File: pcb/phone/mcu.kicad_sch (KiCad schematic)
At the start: 22 parts, among them U1 STM32H743ZIT6, Y1 ECS-80-12-33Q-GN-TR

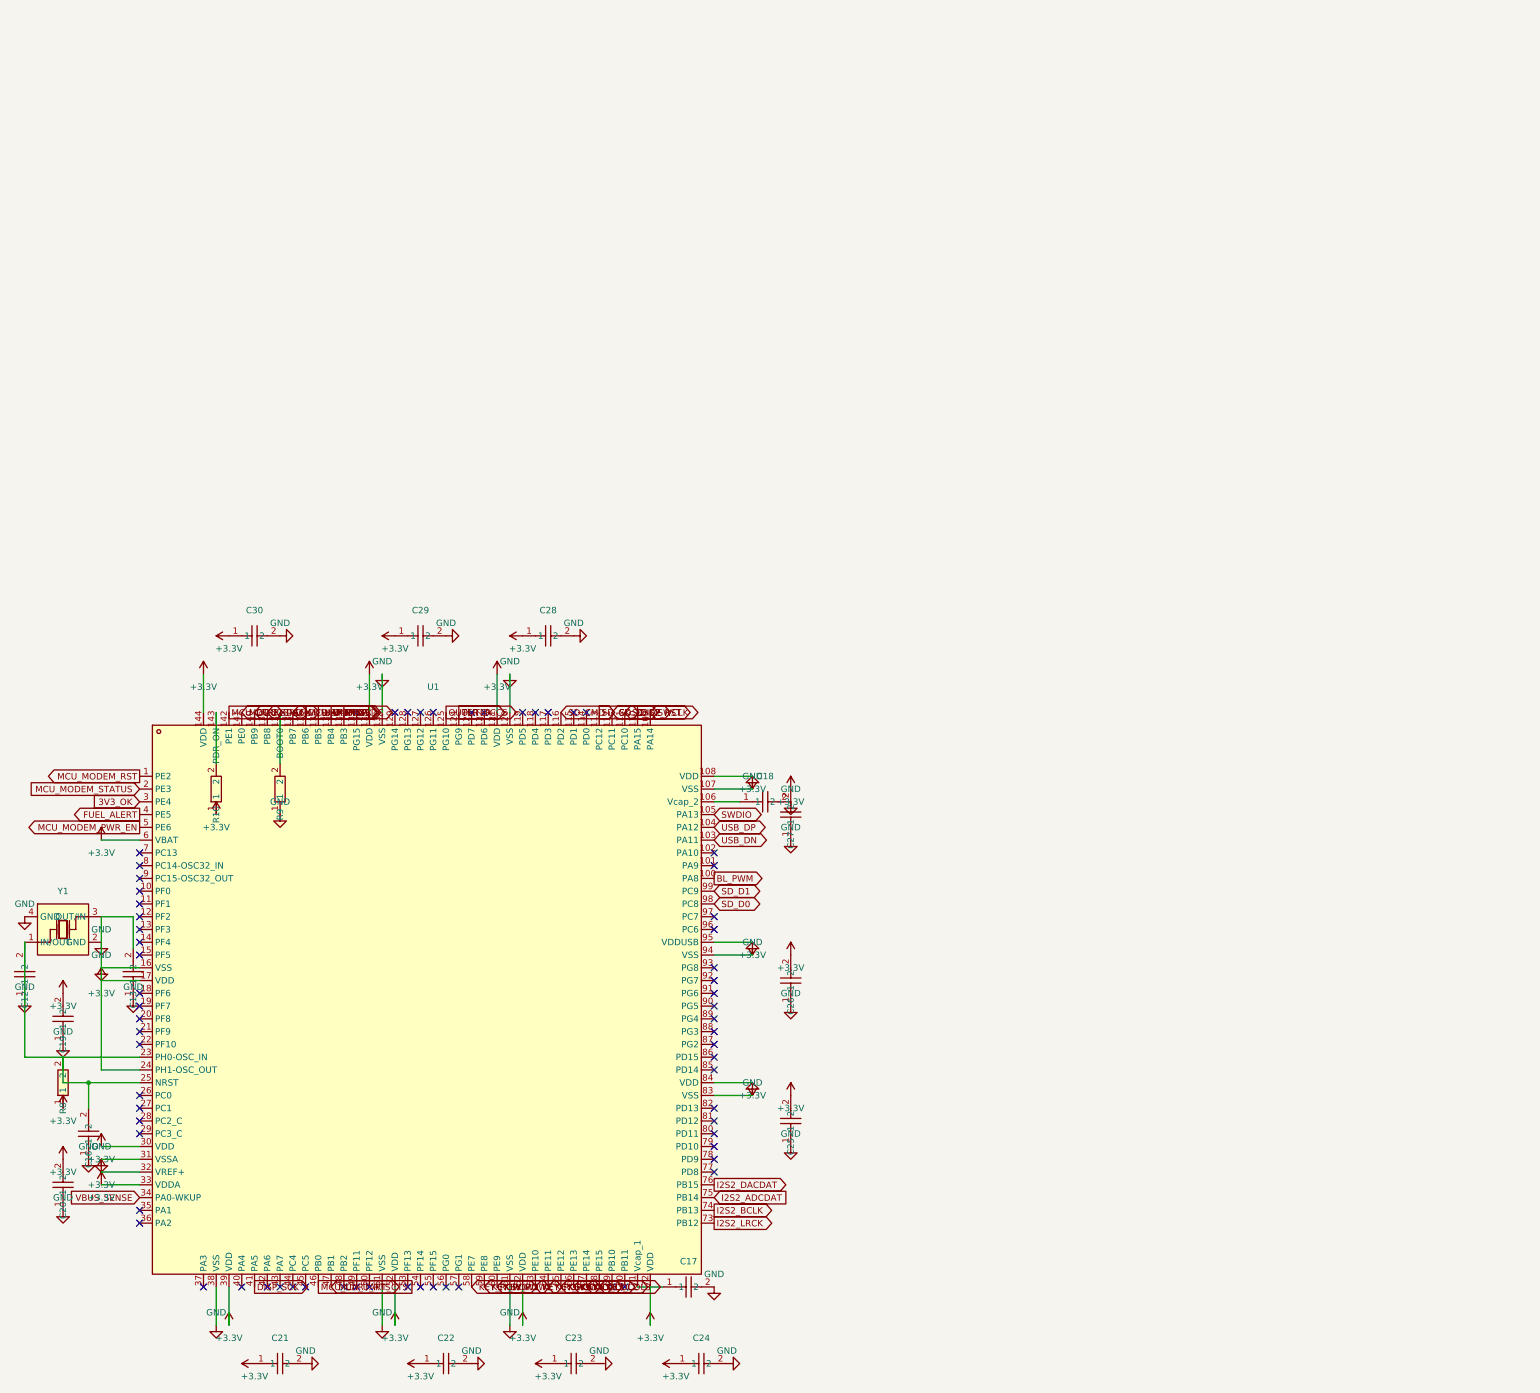
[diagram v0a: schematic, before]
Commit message: Phase 3.3: Complete modem sheet + MCU power symbol cleanup
Modem sheet (modem.kicad_sch):
- MPCIe socket (U2), TXB0108 level shifter (U8), bulk caps (C31/C32), pullup (R11)
- All 54 MPCIe pins wired: power, UART, PCM, USB, SIM, control signals
- Power symbol lib_symbols extracted from KiCad power library
- No PWR_FLAGs (power rails driven by root sheet regulators)
- 0 ERC errors on modem sheet

MCU sheet (mcu.kicad_sch):
- Fixed 14 overlapping power symbol clusters (2.54mm -> 5.08mm+ spacing)
- User manual pass: rotated and spaced components for readability
- ERC unchanged: 5 pre-existing root sheet errors, 0 MCU errors

Generated with [Devin](https://devin.ai)

Co-Authored-By: Devin <158243242+devin-ai-integration[bot]@users.noreply.github.com
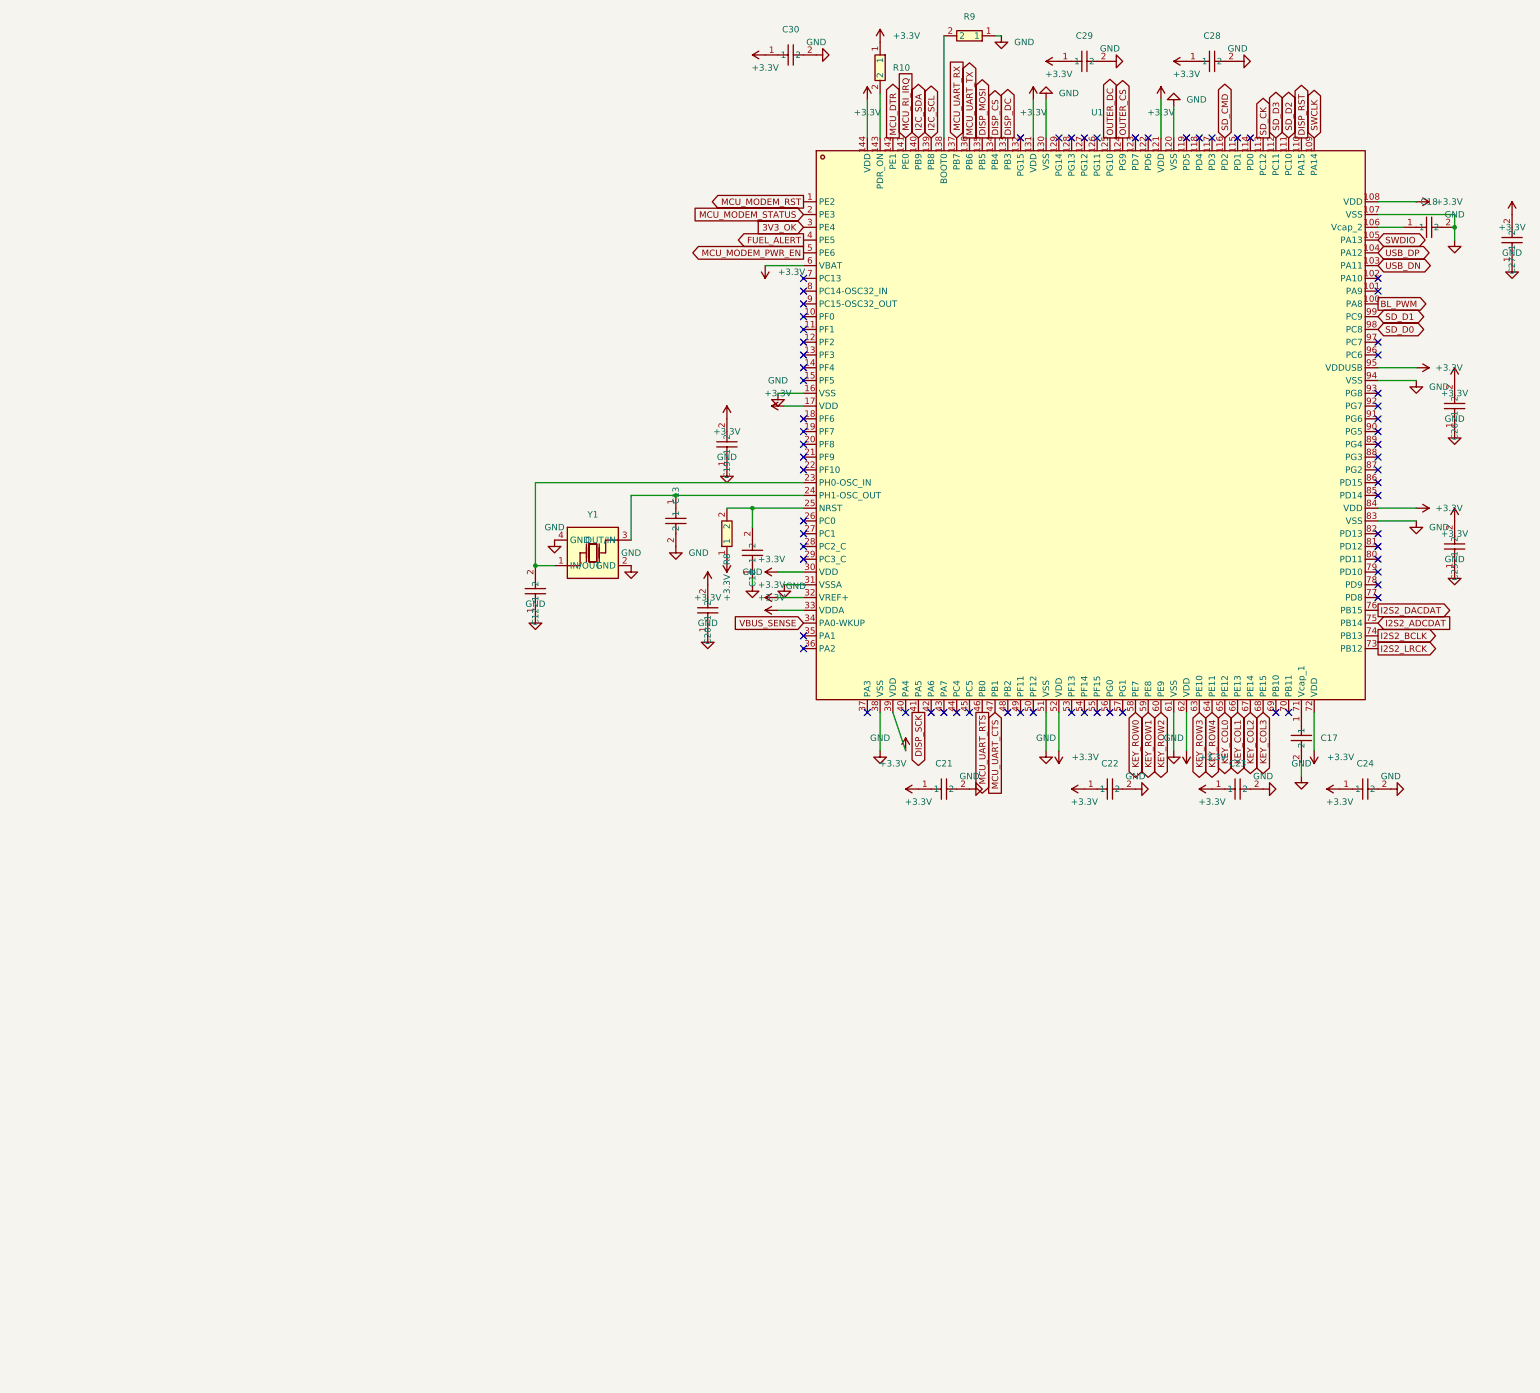
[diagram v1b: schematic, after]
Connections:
- net GND: now also C13.2; no longer C13.1
- net at U1.24 (PH1-OSC_OUT), Y1.3 (OUT/IN): now also C13.1; no longer C13.2
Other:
- moved on the sheet: C12, C13, C16, C17, C18, C19, C20, C21, C22, C23, C24, C25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

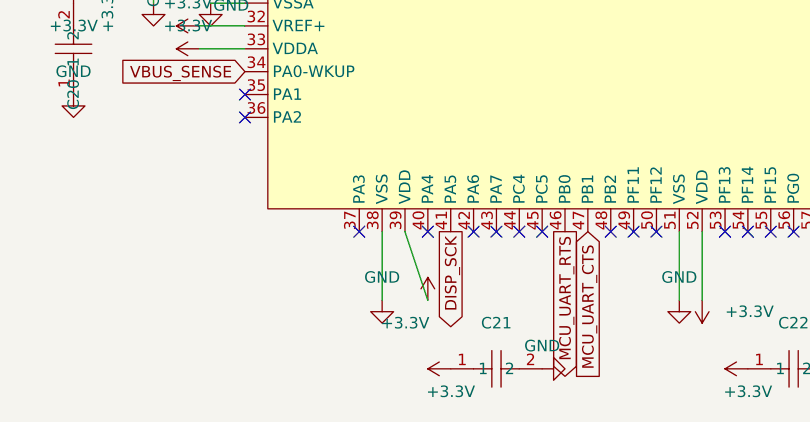
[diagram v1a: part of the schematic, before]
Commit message: User edits: keypad rewiring, sheet reorder, ERC severity reverts, R24 fix
Keypad (keypad.kicad_sch):
- Rotated all 20 switches 270 degrees for vertical contact orientation
- Wired all 4 pins on each switch (pins 1&2 to column, pins 3&4 to row)
- Removed all 37 no_connect markers on pins 3&4
- Cleaned up to 25.4mm (1-inch) grid spacing
- Added pull-down resistors to all 4 columns (was only KEY_COL3)

Root sheet (phone.kicad_sch):
- Reordered sub-sheet blocks (Display_Daughter before SIM_SD)
- Cleaned up PWR_FLAG symbol formatting/indentation
- Reordered PWR_FLAG and +BATT symbol placement

MCU sheet (mcu.kicad_sch):
- Repositioned +3.3V power symbol (#PWR32) at pin 190.5,200.66

Project settings (phone.kicad_pro):
- Reverted ERC suppressions: endpoint_off_grid, isolated_pin_label,
  lib_symbol_mismatch back to warning (want actual fixes, not ignores)
- Added SW2-20 to used designators
- Reordered sheets list (Display_Daughter before SIM_SD)

Other sheets (codec, display, display_daughter, sim_sd):
- KiCad editor reformatting upon save

Generated with [Devin](https://devin.ai)

Co-Authored-By: Devin <158243242+devin-ai-integration[bot]@users.noreply.github.com>
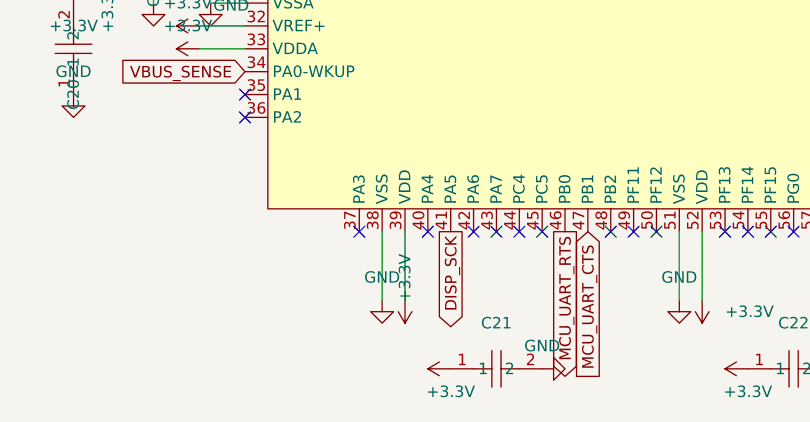
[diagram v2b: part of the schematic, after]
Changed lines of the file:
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@@
 	(wire
 		(pts
-			(xy 190.5 193.04) (xy 193.04 200.66)
+			(xy 190.5 193.04) (xy 190.5 200.66)
 		)
 		(stroke
@@
 	(symbol
 		(lib_id "power:+3.3V")
-		(at 193.04 200.66 0)
+		(at 190.5 200.66 180)
 		(unit 1)
 		(body_style 1)
@@
 		(in_pos_files yes)
 		(dnp no)
-		(fields_autoplaced yes)
 		(property "Reference" "#PWR32"
-			(at 186.69 200.66 0)
+			(at 196.85 200.66 0)
 			(hide yes)
 			(show_name no)
@@
 		)
 		(property "Value" "+3.3V"
-			(at 190.5 203.2 0)
+			(at 190.5 200.914 90)
 			(show_name no)
 			(do_not_autoplace no)
@@
 					(size 1.27 1.27)
 				)
+				(justify right)
 			)
 		)
 		(property "Footprint" ""
-			(at 193.04 200.66 0)
+			(at 190.5 200.66 0)
 			(hide yes)
 			(show_name no)
@@
 		)
 		(property "Datasheet" ""
-			(at 193.04 200.66 0)
+			(at 190.5 200.66 0)
 			(hide yes)
 			(show_name no)
@@
 		)
 		(property "Description" "Power symbol creates a global label with name \"+3.3V\""
-			(at 193.04 200.66 0)
+			(at 190.5 200.66 0)
 			(hide yes)
 			(show_name no)
